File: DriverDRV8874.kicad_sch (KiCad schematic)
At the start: 28 parts, among them J1 Conn_01x06, J2 Conn_01x06, U1 DRV8874PWPR, U11 Green LED, U12 Green LED, U2 DRV8874PWPR

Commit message: Footprints V2
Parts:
- C1: footprint Capacitor_SMD:CP_Elec_6.3x5.4 -> Capacitor_SMD:C_0402_1005Metric_Pad0.74x0.62mm_HandSolder
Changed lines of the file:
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@@
 			)
 		)
-		(property "Footprint" "Capacitor_SMD:CP_Elec_6.3x5.4"
+		(property "Footprint" "Capacitor_SMD:C_0402_1005Metric_Pad0.74x0.62mm_HandSolder"
 			(at 129.2352 62.23 0)
 			(hide yes)

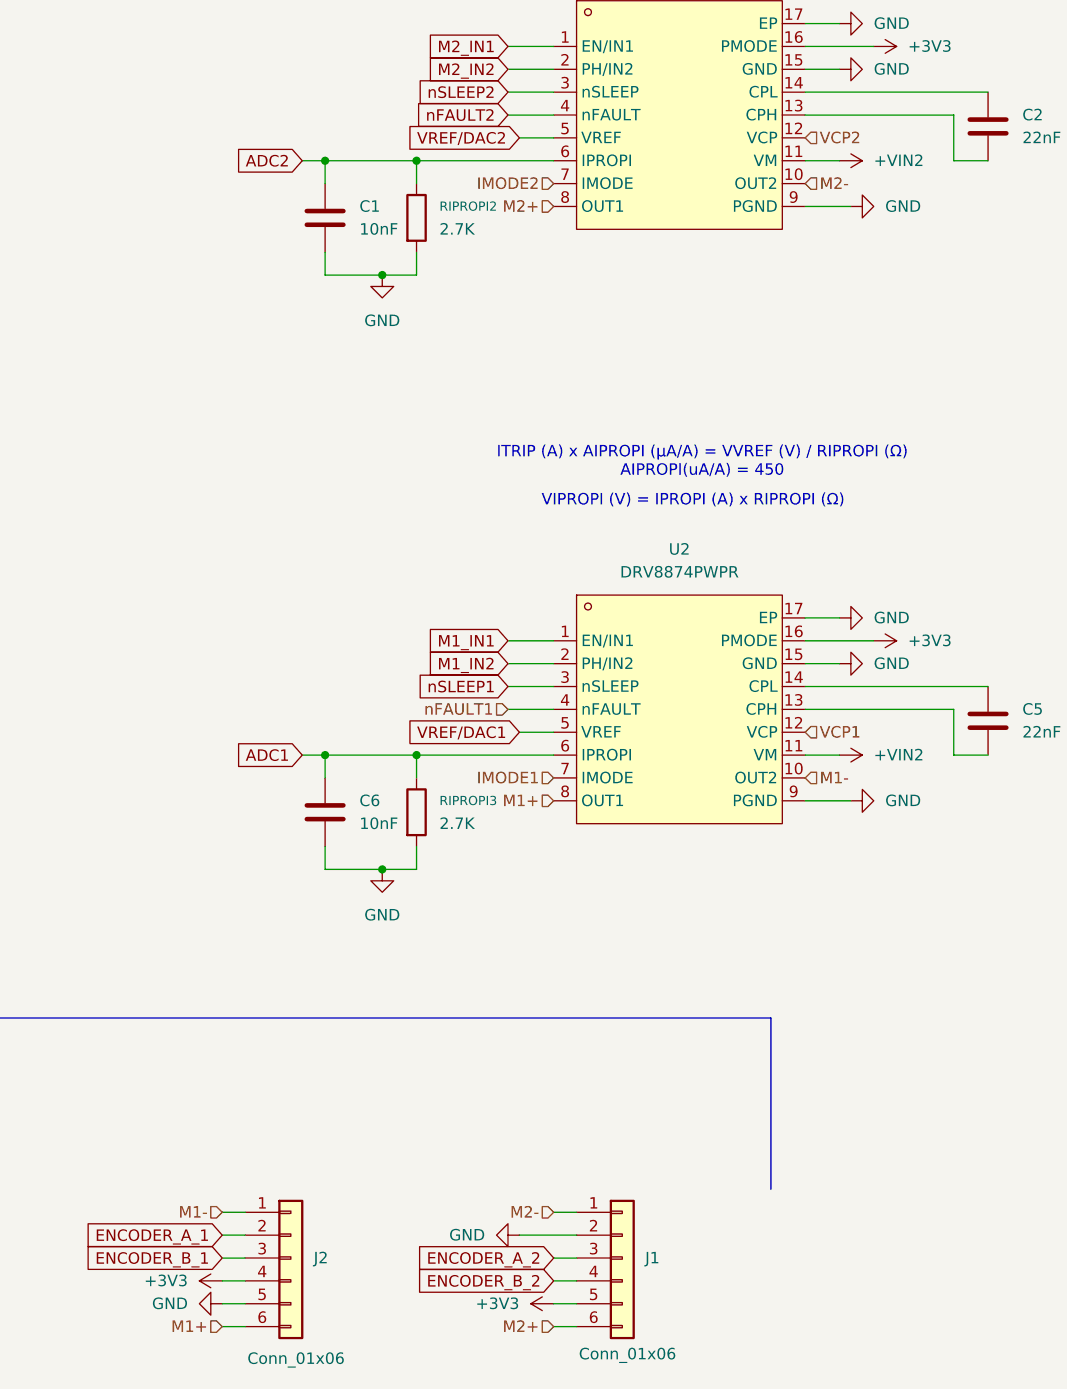
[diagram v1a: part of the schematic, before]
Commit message: Actualización de nets
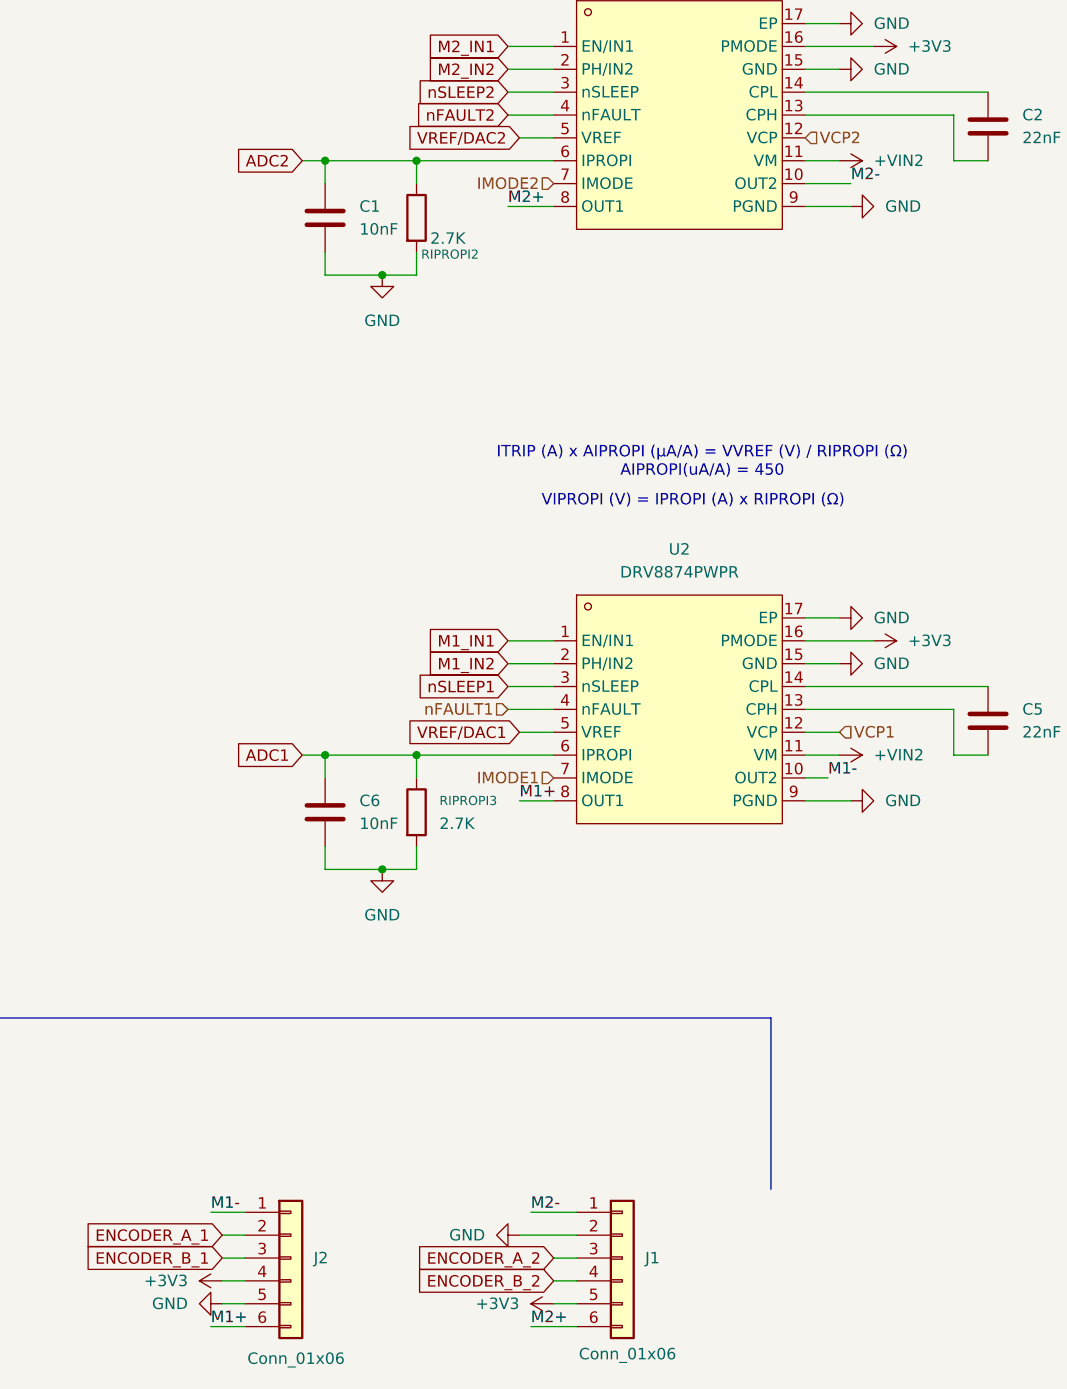
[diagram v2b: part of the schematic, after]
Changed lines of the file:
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@@
 	(wire
 		(pts
+			(xy 151.13 168.91) (xy 156.21 168.91)
+		)
+		(stroke
+			(width 0)
+			(type default)
+		)
+	)
+	(wire
+		(pts
 			(xy 148.59 39.37) (xy 153.67 39.37)
 		)
@@
 	(wire
 		(pts
+			(xy 186.69 54.61) (xy 181.61 54.61)
+		)
+		(stroke
+			(width 0)
+			(type default)
+		)
+	)
+	(wire
+		(pts
 			(xy 181.61 105.41) (xy 189.23 105.41)
 		)
@@
 	(wire
 		(pts
-			(xy 153.67 181.61) (xy 156.21 181.61)
+			(xy 151.13 181.61) (xy 156.21 181.61)
 		)
 		(stroke
@@
 		)
 	)
+	(wire
+		(pts
+			(xy 148.59 57.15) (xy 153.67 57.15)
+		)
+		(stroke
+			(width 0)
+			(type default)
+		)
+	)
 	(polyline
 		(pts
@@
 	(wire
 		(pts
+			(xy 149.86 123.19) (xy 153.67 123.19)
+		)
+		(stroke
+			(width 0)
+			(type default)
+		)
+	)
+	(wire
+		(pts
 			(xy 262.89 29.21) (xy 262.89 35.56)
 		)
@@
 	(wire
 		(pts
-			(xy 138.43 64.77) (xy 138.43 62.23)
+			(xy 184.15 120.65) (xy 181.61 120.65)
 		)
 		(stroke
@@
 	(wire
 		(pts
-			(xy 153.67 168.91) (xy 156.21 168.91)
+			(xy 138.43 64.77) (xy 138.43 62.23)
 		)
 		(stroke
@@
 	(wire
 		(pts
+			(xy 185.42 115.57) (xy 181.61 115.57)
+		)
+		(stroke
+			(width 0)
+			(type default)
+		)
+	)
+	(wire
+		(pts
 			(xy 181.61 44.45) (xy 201.93 44.45)
 		)
@@
 	(wire
 		(pts
-			(xy 116.84 168.91) (xy 119.38 168.91)
+			(xy 115.57 168.91) (xy 119.38 168.91)
 		)
 		(stroke
@@
 	(wire
 		(pts
-			(xy 116.84 181.61) (xy 119.38 181.61)
+			(xy 115.57 181.61) (xy 119.38 181.61)
 		)
 		(stroke
@@
 		)
 	)
+	(label "M1+"
+		(at 149.86 123.19 0)
+		(effects
+			(font
+				(size 1.27 1.27)
+			)
+			(justify left bottom)
+		)
+	)
+	(label "M1-"
+		(at 115.57 168.91 0)
+		(effects
+			(font
+				(size 1.27 1.27)
+			)
+			(justify left bottom)
+		)
+	)
+	(label "M2-"
+		(at 151.13 168.91 0)
+		(effects
+			(font
+				(size 1.27 1.27)
+			)
+			(justify left bottom)
+		)
+	)
+	(label "M1+"
+		(at 115.57 181.61 0)
+		(effects
+			(font
+				(size 1.27 1.27)
+			)
+			(justify left bottom)
+		)
+	)
+	(label "M1-"
+		(at 184.15 120.65 0)
+		(effects
+			(font
+				(size 1.27 1.27)
+			)
+			(justify left bottom)
+		)
+	)
+	(label "M2+"
+		(at 151.13 181.61 0)
+		(effects
+			(font
+				(size 1.27 1.27)
+			)
+			(justify left bottom)
+		)
+	)
+	(label "M2+"
+		(at 148.59 57.15 0)
+		(effects
+			(font
+				(size 1.27 1.27)
+			)
+			(justify left bottom)
+		)
+	)
+	(label "M2-"
+		(at 186.69 54.61 0)
+		(effects
+			(font
+				(size 1.27 1.27)
+			)
+			(justify left bottom)
+		)
+	)
 	(global_label "ADC1"
 		(shape input)
@@
 		)
 	)
-	(hierarchical_label "M2-"
-		(shape input)
-		(at 153.67 168.91 180)
-		(effects
-			(font
-				(size 1.27 1.27)
-			)
-			(justify right)
-		)
-	)
-	(hierarchical_label "M2+"
-		(shape input)
-		(at 153.67 57.15 180)
-		(effects
-			(font
-				(size 1.27 1.27)
-			)
-			(justify right)
-		)
-	)
 	(hierarchical_label "nFAULT2"
 		(shape input)
@@
 	(hierarchical_label "VCP1"
 		(shape input)
-		(at 181.61 115.57 0)
+		(at 185.42 115.57 0)
 		(effects
 			(font
@@
 		)
 	)
-	(hierarchical_label "M2+"
-		(shape input)
-		(at 153.67 181.61 180)
-		(effects
-			(font
-				(size 1.27 1.27)
-			)
-			(justify right)
-		)
-	)
-	(hierarchical_label "M2-"
-		(shape input)
-		(at 181.61 54.61 0)
-		(effects
-			(font
-				(size 1.27 1.27)
-			)
-			(justify left)
-		)
-	)
 	(hierarchical_label "IMODE1"
 		(shape input)
@@
 		)
 	)
-	(hierarchical_label "M1+"
-		(shape input)
-		(at 116.84 181.61 180)
-		(effects
-			(font
-				(size 1.27 1.27)
-			)
-			(justify right)
-		)
-	)
-	(hierarchical_label "M1-"
-		(shape input)
-		(at 181.61 120.65 0)
-		(effects
-			(font
-				(size 1.27 1.27)
-			)
-			(justify left)
-		)
-	)
 	(hierarchical_label "VCP2"
 		(shape input)
@@
 		)
 	)
-	(hierarchical_label "M1-"
-		(shape input)
-		(at 116.84 168.91 180)
-		(effects
-			(font
-				(size 1.27 1.27)
-			)
-			(justify right)
-		)
-	)
 	(hierarchical_label "VCP1"
 		(shape input)
@@
 		)
 	)
-	(hierarchical_label "M1+"
-		(shape input)
-		(at 153.67 123.19 180)
-		(effects
-			(font
-				(size 1.27 1.27)
-			)
-			(justify right)
-		)
-	)
 	(symbol
 		(lib_id "power:+5V")
@@
 		(in_pos_files yes)
 		(dnp no)
-		(fields_autoplaced yes)
 		(property "Reference" "RIPROPI2"
-			(at 140.97 57.1499 0)
+			(at 138.938 62.484 0)
 			(show_name no)
 			(do_not_autoplace no)
@@
 		)
 		(property "Value" "2.7K"
-			(at 140.97 59.6899 0)
+			(at 139.954 60.706 0)
 			(show_name no)
 			(do_not_autoplace no)

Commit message: Cantidad de errores en la PCB: 29
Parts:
- C33, C34, C35, C36: footprint easyeda2kicad:C0402 -> ARLISS-footprints:C0402
- D3: footprint easyeda2kicad:SMB_L4.3-W3.6-LS5.3-RD -> ARLISS-footprints:SMB_L4.3-W3.6-LS5.3-RD
- U1, U2: footprint easyeda2kicad:HTSSOP-16_L5.0-W4.4-P0.65-LS6.4-BL-EP -> ARLISS-footprints:HTSSOP-16_L5.0-W4.4-P0.65-LS6.4-BL-EP
- U12: footprint easyeda2kicad:LED0603-FD -> ARLISS-footprints:LED0603-FD
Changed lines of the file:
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@@
 			)
 		)
-		(property "Footprint" "easyeda2kicad:SMB_L4.3-W3.6-LS5.3-RD"
+		(property "Footprint" "ARLISS-footprints:SMB_L4.3-W3.6-LS5.3-RD"
 			(at 217.17 69.85 0)
 			(hide yes)
@@
 			)
 		)
-		(property "Footprint" "easyeda2kicad:HTSSOP-16_L5.0-W4.4-P0.65-LS6.4-BL-EP"
+		(property "Footprint" "ARLISS-footprints:HTSSOP-16_L5.0-W4.4-P0.65-LS6.4-BL-EP"
 			(at 167.64 64.77 0)
 			(hide yes)
@@
 			)
 		)
-		(property "Footprint" "easyeda2kicad:LED0603-FD"
+		(property "Footprint" "ARLISS-footprints:LED0603-FD"
 			(at 214.63 38.1 0)
 			(hide yes)
@@
 			)
 		)
-		(property "Footprint" "easyeda2kicad:C0402"
+		(property "Footprint" "ARLISS-footprints:C0402"
 			(at 267.97 71.12 0)
 			(hide yes)
@@
 			)
 		)
-		(property "Footprint" "easyeda2kicad:C0402"
+		(property "Footprint" "ARLISS-footprints:C0402"
 			(at 265.43 143.51 0)
 			(hide yes)
@@
 			)
 		)
-		(property "Footprint" "easyeda2kicad:C0402"
+		(property "Footprint" "ARLISS-footprints:C0402"
 			(at 252.73 143.51 0)
 			(hide yes)
@@
 			)
 		)
-		(property "Footprint" "easyeda2kicad:C0402"
+		(property "Footprint" "ARLISS-footprints:C0402"
 			(at 255.27 71.12 0)
 			(hide yes)
@@
 			)
 		)
-		(property "Footprint" "easyeda2kicad:HTSSOP-16_L5.0-W4.4-P0.65-LS6.4-BL-EP"
+		(property "Footprint" "ARLISS-footprints:HTSSOP-16_L5.0-W4.4-P0.65-LS6.4-BL-EP"
 			(at 167.64 130.81 0)
 			(hide yes)

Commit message: Cantidad de errores de la placa: 05
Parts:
- C3, C4: footprint easyeda2kicad:CAP-SMD_BD6.3-L6.6-W6.6-FD -> ARLISS-footprints:CAP-SMD_BD6.3-L6.6-W6.6-FD
- D6: footprint easyeda2kicad:SMB_L4.3-W3.6-LS5.3-RD -> ARLISS-footprints:SMB_L4.3-W3.6-LS5.3-RD
- U11: footprint easyeda2kicad:LED0603-FD -> ARLISS-footprints:LED0603-FD
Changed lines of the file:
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@@
 			)
 		)
-		(property "Footprint" "easyeda2kicad:LED0603-FD"
+		(property "Footprint" "ARLISS-footprints:LED0603-FD"
 			(at 231.14 111.76 0)
 			(hide yes)
@@
 			)
 		)
-		(property "Footprint" "easyeda2kicad:SMB_L4.3-W3.6-LS5.3-RD"
+		(property "Footprint" "ARLISS-footprints:SMB_L4.3-W3.6-LS5.3-RD"
 			(at 214.63 142.24 0)
 			(hide yes)
@@
 			)
 		)
-		(property "Footprint" "easyeda2kicad:CAP-SMD_BD6.3-L6.6-W6.6-FD"
+		(property "Footprint" "ARLISS-footprints:CAP-SMD_BD6.3-L6.6-W6.6-FD"
 			(at 220.98 152.4 0)
 			(hide yes)
@@
 			)
 		)
-		(property "Footprint" "easyeda2kicad:CAP-SMD_BD6.3-L6.6-W6.6-FD"
+		(property "Footprint" "ARLISS-footprints:CAP-SMD_BD6.3-L6.6-W6.6-FD"
 			(at 226.06 80.01 0)
 			(hide yes)

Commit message: Cantidad de errores en la placa: 04
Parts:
- JP2, JP3: footprint (none) -> Jumper:SolderJumper-2_P1.3mm_Open_TrianglePad1.0x1.5mm
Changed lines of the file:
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@@
 			)
 		)
-		(property "Footprint" ""
+		(property "Footprint" "Jumper:SolderJumper-2_P1.3mm_Open_TrianglePad1.0x1.5mm"
 			(at 238.76 123.19 0)
 			(hide yes)
@@
 			)
 		)
-		(property "Footprint" ""
+		(property "Footprint" "Jumper:SolderJumper-2_P1.3mm_Open_TrianglePad1.0x1.5mm"
 			(at 222.25 49.53 0)
 			(hide yes)

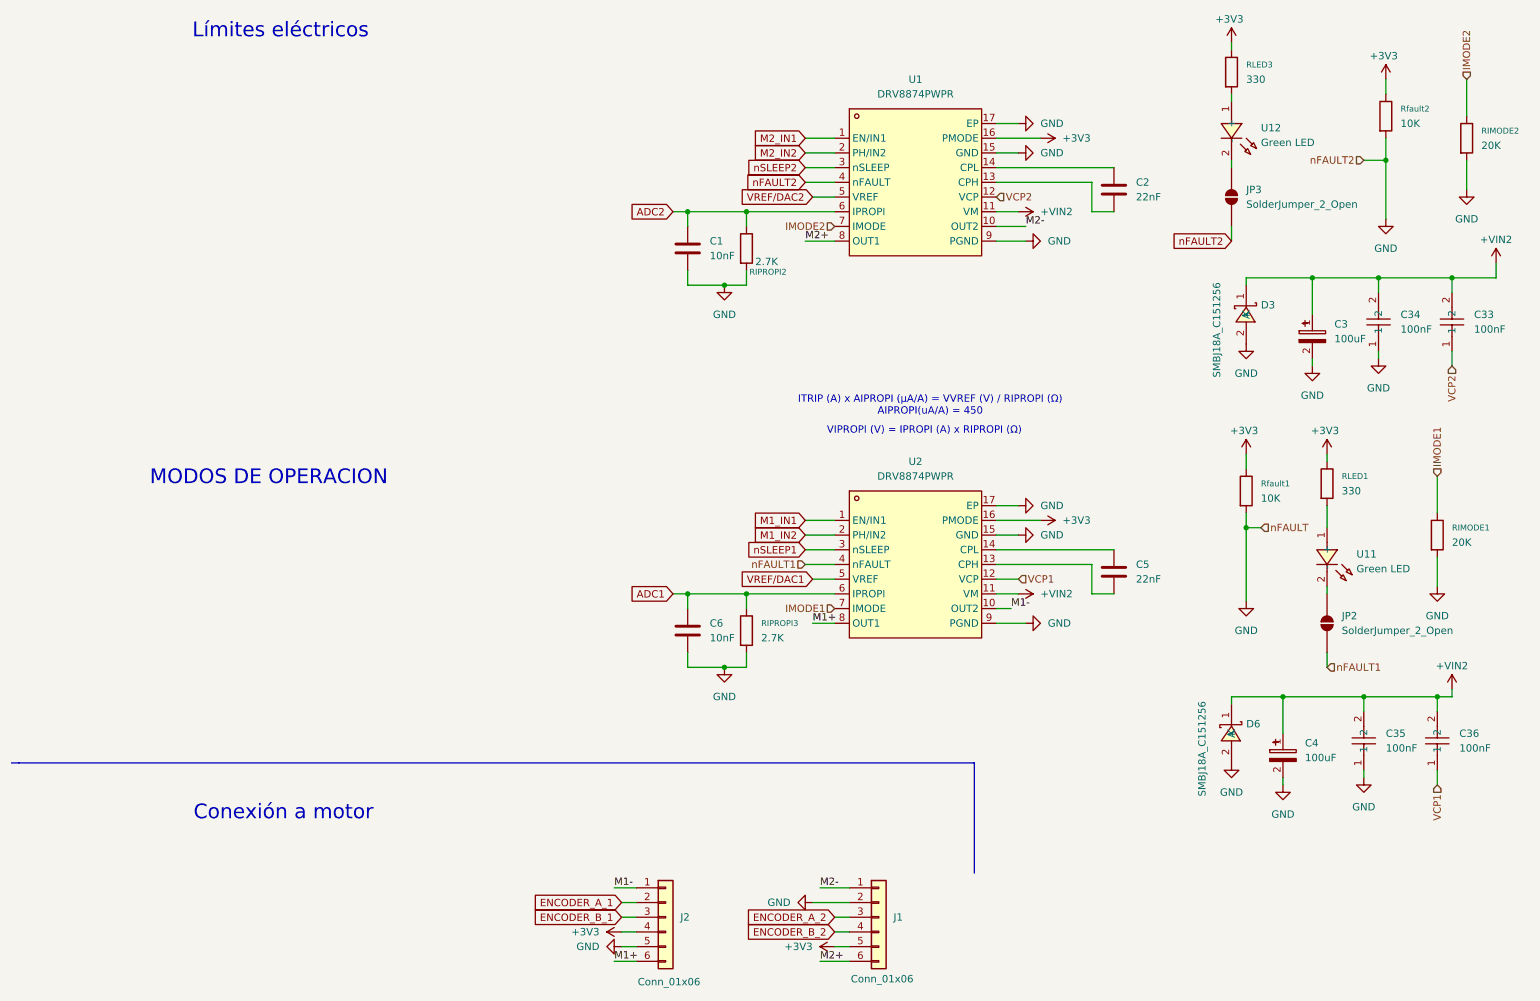
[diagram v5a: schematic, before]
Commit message: Esquemático Versión mejorada
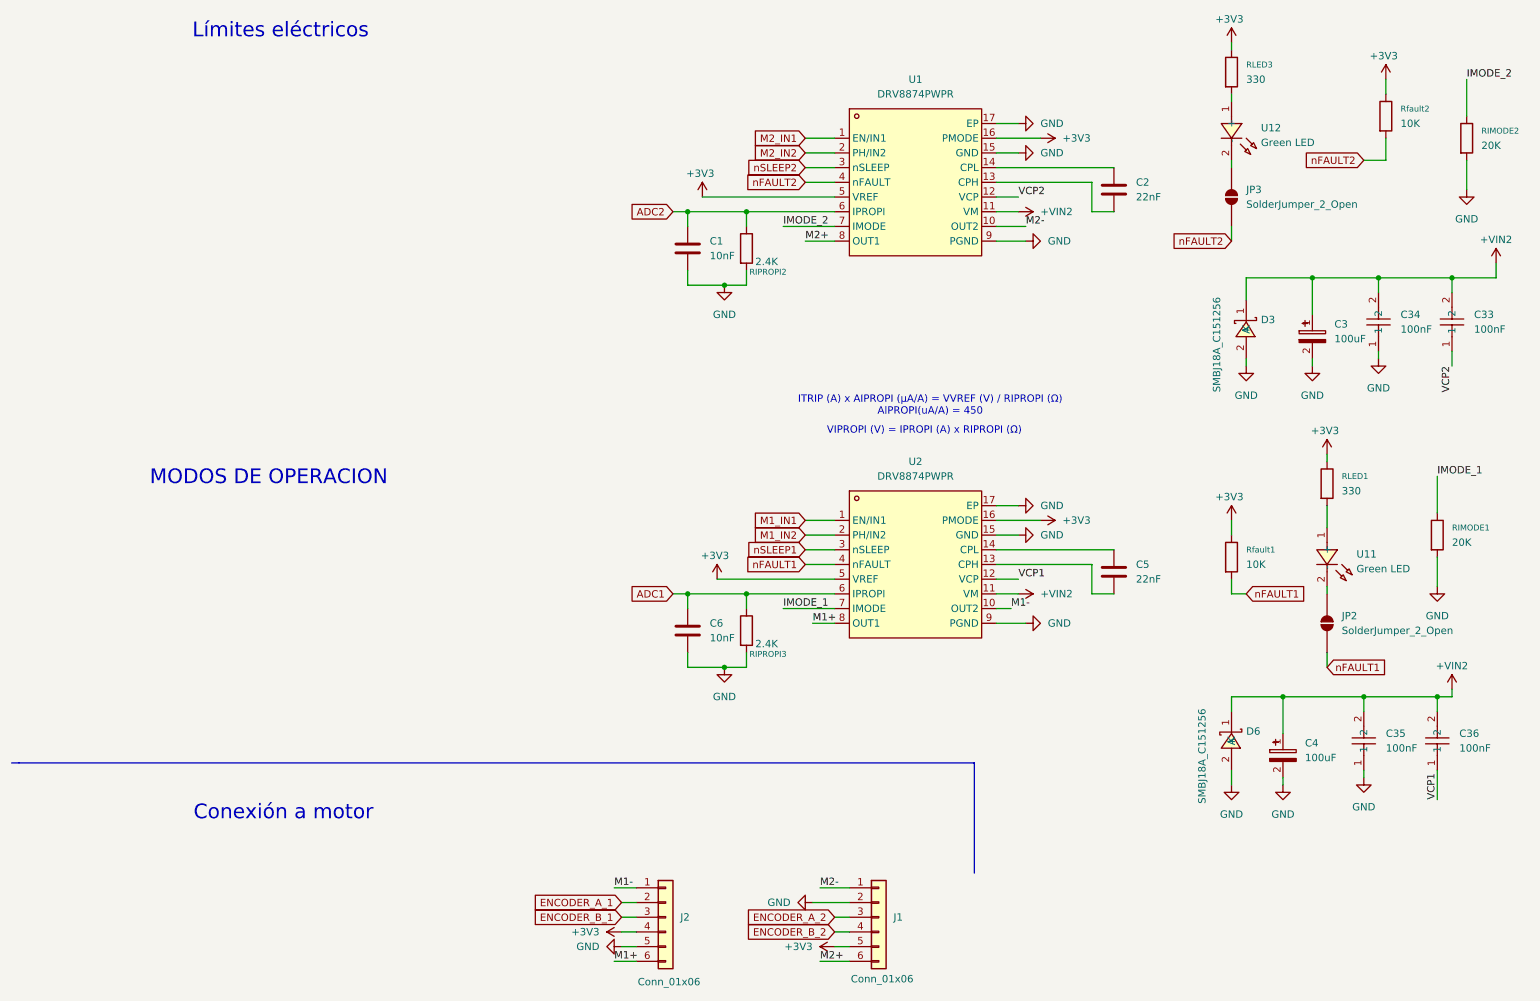
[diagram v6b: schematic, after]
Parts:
- RIPROPI2, RIPROPI3: value 2.7K -> 2.4K; LCSC C19632297 -> C114611
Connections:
- net VREF/DAC1 is gone; now on net +3V3: U2.5 (VREF)
- net VREF/DAC2 is gone; now on net +3V3: U1.5 (VREF)
- net GND: no longer JP3.1 (A), Rfault1.2, Rfault2.2, U1.4 (nFAULT)
- net nFAULT1: now also Rfault1.2
- net IMODE1 renamed IMODE_1
- net IMODE2 renamed IMODE_2
- new net nFAULT2: JP3.1 (A), Rfault2.2, U1.4 (nFAULT)
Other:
- moved on the sheet: D3, D6, Rfault1

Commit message: PCB ordenada V1
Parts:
- added C37, C39: 100nF, ARLISS-footprints:C0402, symbol CANSAT_STM32_symbols:TCC0402X7R104J500AT
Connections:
- net +3V3: now also C37.1, C39.1
- net GND: now also C37.2, C39.2
